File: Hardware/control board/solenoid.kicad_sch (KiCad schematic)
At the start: 7 parts, among them J11 Screw_Terminal_01x02, Q3 NMOS

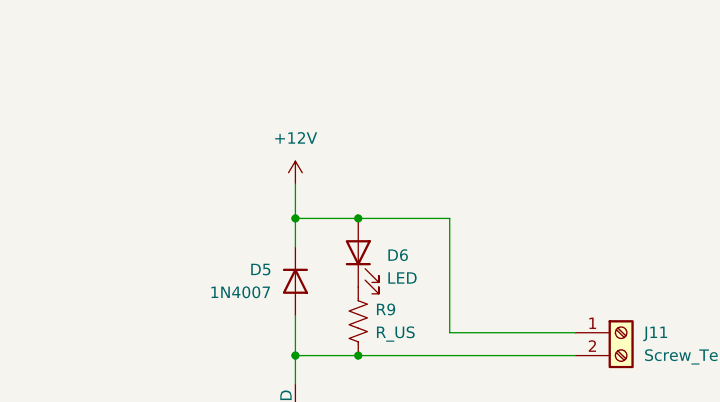
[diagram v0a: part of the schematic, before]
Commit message: added fuses into solenoids/escs
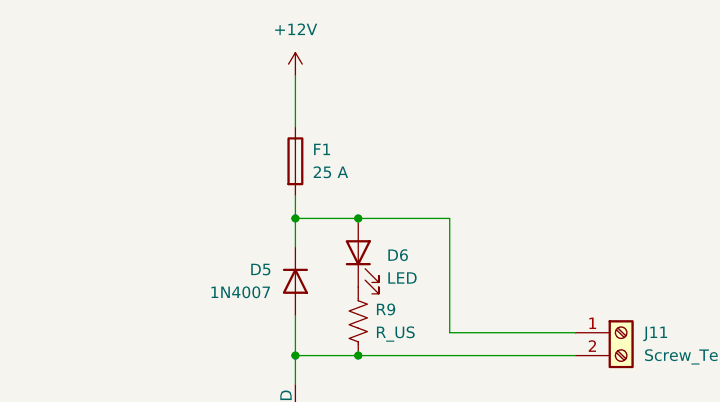
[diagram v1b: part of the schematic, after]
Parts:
- added F1: 25 A, symbol Device:Fuse
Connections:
- net +12V: now also F1.1; no longer D5.1 (K), D6.2 (A), J11.1 (Pin_1)
- new net: D5.1 (K), D6.2 (A), F1.2, J11.1 (Pin_1)
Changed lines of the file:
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@@
 (kicad_sch (version 20230121) (generator eeschema)
   (paper "A4")
+  (junction (at 122.555 75.565) (diameter 0) (color 0 0 0 0)
+  )
   (junction (at 129.54 75.565) (diameter 0) (color 0 0 0 0)
   )
@@
   (junction (at 129.54 90.805) (diameter 0) (color 0 0 0 0)
   )
-  (junction (at 122.555 75.565) (diameter 0) (color 0 0 0 0)
-  )
   (wire (pts (xy 120.015 113.03) (xy 122.555 113.03))
     (stroke (width 0) (type default))
@@
     (stroke (width 0) (type default))
   )
+  (wire (pts (xy 122.555 73.025) (xy 122.555 75.565))
+    (stroke (width 0) (type default))
+  )
   (wire (pts (xy 122.555 104.14) (xy 122.555 113.03))
     (stroke (width 0) (type default))
@@
     (stroke (width 0) (type default))
   )
+  (wire (pts (xy 122.555 59.69) (xy 122.555 65.405))
+    (stroke (width 0) (type default))
+  )
   (wire (pts (xy 139.7 88.265) (xy 153.67 88.265))
-    (stroke (width 0) (type default))
-  )
-  (wire (pts (xy 122.555 71.755) (xy 122.555 75.565))
     (stroke (width 0) (type default))
   )
@@
     (pin "3")
     (instances
-      (project "control board"
-        (path "/cf0863a8-7f64-449b-8eb4-3c06c871fb37"
+      (project "solenoid"
+        (path "/b4ed5960-473e-41d7-9d87-eb439ed22219"
           (reference "Q3") (unit 1)
         )
+      )
+      (project "control board"
+        (path "/cf0863a8-7f64-449b-8eb4-3c06c871fb37"
+          (reference "Q3") (unit 1)
+        )
         (path "/cf0863a8-7f64-449b-8eb4-3c06c871fb37/9fd0b45f-6f46-40af-ae0d-29c33b45e498"
           (reference "Q1") (unit 1)
@@
         (path "/cf0863a8-7f64-449b-8eb4-3c06c871fb37/f39ce93b-3626-4dde-a021-b00a2c8134c7"
           (reference "Q3") (unit 1)
+        )
+      )
+    )
+  )
+  (symbol (lib_id "Device:Fuse") (at 122.555 69.215 0) (unit 1)
+    (in_bom yes) (on_board yes) (dnp no) (fields_autoplaced)
+    (property "Reference" "F1" (at 124.46 67.945 0)
+      (effects (font (size 1.27 1.27)) (justify left))
+    )
+    (property "Value" "25 A" (at 124.46 70.485 0)
+      (effects (font (size 1.27 1.27)) (justify left))
+    )
+    (property "Footprint" "" (at 120.777 69.215 90)
+      (effects (font (size 1.27 1.27)) hide)
+    )
+    (property "Datasheet" "~" (at 122.555 69.215 0)
+      (effects (font (size 1.27 1.27)) hide)
+    )
+    (pin "1")
+    (pin "2")
+    (instances
+      (project "solenoid"
+        (path "/b4ed5960-473e-41d7-9d87-eb439ed22219"
+          (reference "F1") (unit 1)
+        )
+      )
+      (project "control board"
+        (path "/cf0863a8-7f64-449b-8eb4-3c06c871fb37/9fd0b45f-6f46-40af-ae0d-29c33b45e498"
+          (reference "F1") (unit 1)
+        )
+        (path "/cf0863a8-7f64-449b-8eb4-3c06c871fb37/6163a064-c95f-47b6-9c17-0e18c391c233"
+          (reference "F1") (unit 1)
+        )
+        (path "/cf0863a8-7f64-449b-8eb4-3c06c871fb37/f39ce93b-3626-4dde-a021-b00a2c8134c7"
+          (reference "F1") (unit 1)
         )
       )
@@
     (pin "2")
     (instances
-      (project "control board"
-        (path "/cf0863a8-7f64-449b-8eb4-3c06c871fb37"
+      (project "solenoid"
+        (path "/b4ed5960-473e-41d7-9d87-eb439ed22219"
           (reference "D6") (unit 1)
         )
+      )
+      (project "control board"
+        (path "/cf0863a8-7f64-449b-8eb4-3c06c871fb37"
+          (reference "D6") (unit 1)
+        )
         (path "/cf0863a8-7f64-449b-8eb4-3c06c871fb37/9fd0b45f-6f46-40af-ae0d-29c33b45e498"
           (reference "D2") (unit 1)
@@
     (pin "2")
     (instances
-      (project "control board"
-        (path "/cf0863a8-7f64-449b-8eb4-3c06c871fb37"
+      (project "solenoid"
+        (path "/b4ed5960-473e-41d7-9d87-eb439ed22219"
           (reference "J11") (unit 1)
         )
+      )
+      (project "control board"
+        (path "/cf0863a8-7f64-449b-8eb4-3c06c871fb37"
+          (reference "J11") (unit 1)
+        )
         (path "/cf0863a8-7f64-449b-8eb4-3c06c871fb37/9fd0b45f-6f46-40af-ae0d-29c33b45e498"
           (reference "J9") (unit 1)
@@
         (path "/cf0863a8-7f64-449b-8eb4-3c06c871fb37/f39ce93b-3626-4dde-a021-b00a2c8134c7"
           (reference "J11") (unit 1)
-        )
-      )
-    )
-  )
-  (symbol (lib_id "power:+12V") (at 122.555 71.755 0) (unit 1)
-    (in_bom yes) (on_board yes) (dnp no) (fields_autoplaced)
-    (property "Reference" "#PWR08" (at 122.555 75.565 0)
-      (effects (font (size 1.27 1.27)) hide)
-    )
-    (property "Value" "+12V" (at 122.555 66.675 0)
-      (effects (font (size 1.27 1.27)))
-    )
-    (property "Footprint" "" (at 122.555 71.755 0)
-      (effects (font (size 1.27 1.27)) hide)
-    )
-    (property "Datasheet" "" (at 122.555 71.755 0)
-      (effects (font (size 1.27 1.27)) hide)
-    )
-    (pin "1")
-    (instances
-      (project "control board"
-        (path "/cf0863a8-7f64-449b-8eb4-3c06c871fb37"
-          (reference "#PWR08") (unit 1)
-        )
-        (path "/cf0863a8-7f64-449b-8eb4-3c06c871fb37/9fd0b45f-6f46-40af-ae0d-29c33b45e498"
-          (reference "#PWR02") (unit 1)
-        )
-        (path "/cf0863a8-7f64-449b-8eb4-3c06c871fb37/6163a064-c95f-47b6-9c17-0e18c391c233"
-          (reference "#PWR04") (unit 1)
-        )
-        (path "/cf0863a8-7f64-449b-8eb4-3c06c871fb37/f39ce93b-3626-4dde-a021-b00a2c8134c7"
-          (reference "#PWR06") (unit 1)
         )
       )
@@
     (pin "2")
     (instances
-      (project "control board"
-        (path "/cf0863a8-7f64-449b-8eb4-3c06c871fb37"
+      (project "solenoid"
+        (path "/b4ed5960-473e-41d7-9d87-eb439ed22219"
           (reference "R8") (unit 1)
         )
+      )
+      (project "control board"
+        (path "/cf0863a8-7f64-449b-8eb4-3c06c871fb37"
+          (reference "R8") (unit 1)
+        )
         (path "/cf0863a8-7f64-449b-8eb4-3c06c871fb37/9fd0b45f-6f46-40af-ae0d-29c33b45e498"
           (reference "R2") (unit 1)
@@
     (pin "2")
     (instances
+      (project "solenoid"
+        (path "/b4ed5960-473e-41d7-9d87-eb439ed22219"
+          (reference "R9") (unit 1)
+        )
+      )
       (project "control board"
         (path "/cf0863a8-7f64-449b-8eb4-3c06c871fb37"
@@
     (pin "1")
     (instances
+      (project "solenoid"
+        (path "/b4ed5960-473e-41d7-9d87-eb439ed22219"
+          (reference "#PWR09") (unit 1)
+        )
+      )
       (project "control board"
         (path "/cf0863a8-7f64-449b-8eb4-3c06c871fb37"
@@
     (pin "2")
     (instances
-      (project "control board"
-        (path "/cf0863a8-7f64-449b-8eb4-3c06c871fb37"
+      (project "solenoid"
+        (path "/b4ed5960-473e-41d7-9d87-eb439ed22219"
           (reference "R7") (unit 1)
         )
+      )
+      (project "control board"
+        (path "/cf0863a8-7f64-449b-8eb4-3c06c871fb37"
+          (reference "R7") (unit 1)
+        )
         (path "/cf0863a8-7f64-449b-8eb4-3c06c871fb37/9fd0b45f-6f46-40af-ae0d-29c33b45e498"
           (reference "R1") (unit 1)
@@
         (path "/cf0863a8-7f64-449b-8eb4-3c06c871fb37/f39ce93b-3626-4dde-a021-b00a2c8134c7"
           (reference "R7") (unit 1)
+        )
+      )
+    )
+  )
+  (symbol (lib_id "power:+12V") (at 122.555 59.69 0) (unit 1)
+    (in_bom yes) (on_board yes) (dnp no) (fields_autoplaced)
+    (property "Reference" "#PWR01" (at 122.555 63.5 0)
+      (effects (font (size 1.27 1.27)) hide)
+    )
+    (property "Value" "+12V" (at 122.555 54.61 0)
+      (effects (font (size 1.27 1.27)))
+    )
+    (property "Footprint" "" (at 122.555 59.69 0)
+      (effects (font (size 1.27 1.27)) hide)
+    )
+    (property "Datasheet" "" (at 122.555 59.69 0)
+      (effects (font (size 1.27 1.27)) hide)
+    )
+    (pin "1")
+    (instances
+      (project "solenoid"
+        (path "/b4ed5960-473e-41d7-9d87-eb439ed22219"
+          (reference "#PWR01") (unit 1)
+        )
+      )
+      (project "control board"
+        (path "/cf0863a8-7f64-449b-8eb4-3c06c871fb37/9fd0b45f-6f46-40af-ae0d-29c33b45e498"
+          (reference "#PWR01") (unit 1)
+        )
+        (path "/cf0863a8-7f64-449b-8eb4-3c06c871fb37/6163a064-c95f-47b6-9c17-0e18c391c233"
+          (reference "#PWR01") (unit 1)
+        )
+        (path "/cf0863a8-7f64-449b-8eb4-3c06c871fb37/f39ce93b-3626-4dde-a021-b00a2c8134c7"
+          (reference "#PWR01") (unit 1)
         )
       )
@@
     (pin "2")
     (instances
-      (project "control board"
-        (path "/cf0863a8-7f64-449b-8eb4-3c06c871fb37"
+      (project "solenoid"
+        (path "/b4ed5960-473e-41d7-9d87-eb439ed22219"
+          (reference "D5") (unit 1)
+        )
+      )
+      (project "control board"
+        (path "/cf0863a8-7f64-449b-8eb4-3c06c871fb37"

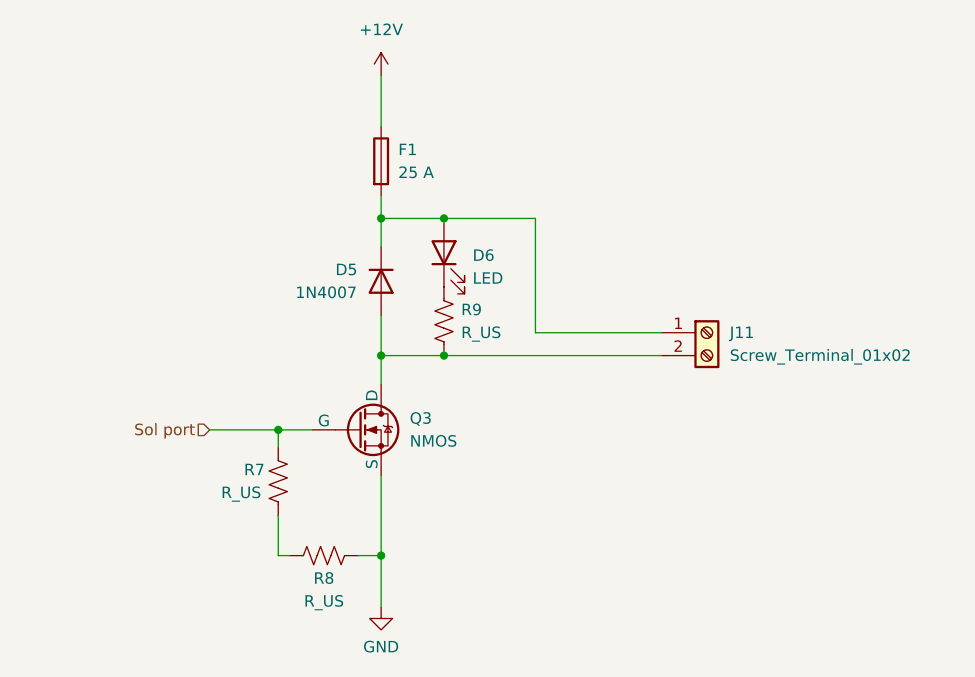
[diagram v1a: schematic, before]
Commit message: renamed boards
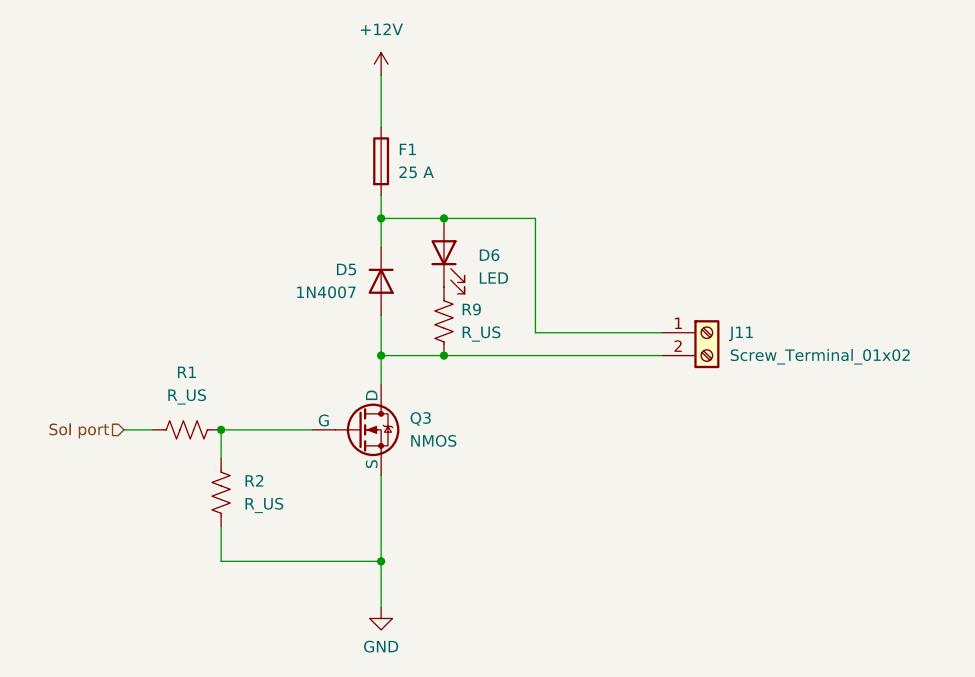
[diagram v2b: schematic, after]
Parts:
- removed R7, R8: R_US, symbol Device:R_US
- added R1, R2: R_US, symbol Device:R_US
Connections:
- net GND: now also R2.2
- net Sol port: now also R1.1; no longer Q3.2 (G)
- new net: Q3.2 (G), R1.2, R2.1
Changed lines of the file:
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@@
   (junction (at 122.555 90.805) (diameter 0) (color 0 0 0 0)
   )
-  (junction (at 122.555 113.03) (diameter 0) (color 0 0 0 0)
-  )
-  (junction (at 111.125 99.06) (diameter 0) (color 0 0 0 0)
+  (junction (at 104.775 99.06) (diameter 0) (color 0 0 0 0)
+  )
+  (junction (at 122.555 113.665) (diameter 0) (color 0 0 0 0)
   )
   (junction (at 129.54 90.805) (diameter 0) (color 0 0 0 0)
   )
-  (wire (pts (xy 120.015 113.03) (xy 122.555 113.03))
+  (wire (pts (xy 104.775 109.855) (xy 104.775 113.665))
+    (stroke (width 0) (type default))
+  )
+  (wire (pts (xy 104.775 99.06) (xy 104.775 102.235))
     (stroke (width 0) (type default))
   )
@@
     (stroke (width 0) (type default))
   )
-  (wire (pts (xy 111.125 108.585) (xy 111.125 113.03))
-    (stroke (width 0) (type default))
-  )
-  (wire (pts (xy 111.125 113.03) (xy 112.395 113.03))
+  (wire (pts (xy 104.775 99.06) (xy 114.935 99.06))
+    (stroke (width 0) (type default))
+  )
+  (wire (pts (xy 104.775 113.665) (xy 122.555 113.665))
     (stroke (width 0) (type default))
   )
@@
     (stroke (width 0) (type default))
   )
-  (wire (pts (xy 103.505 99.06) (xy 111.125 99.06))
+  (wire (pts (xy 93.98 99.06) (xy 97.155 99.06))
     (stroke (width 0) (type default))
   )
@@
     (stroke (width 0) (type default))
   )
-  (wire (pts (xy 111.125 99.06) (xy 111.125 100.965))
-    (stroke (width 0) (type default))
-  )
   (wire (pts (xy 122.555 73.025) (xy 122.555 75.565))
     (stroke (width 0) (type default))
   )
-  (wire (pts (xy 122.555 104.14) (xy 122.555 113.03))
-    (stroke (width 0) (type default))
-  )
   (wire (pts (xy 129.54 75.565) (xy 139.7 75.565))
     (stroke (width 0) (type default))
@@
     (stroke (width 0) (type default))
   )
-  (wire (pts (xy 111.125 99.06) (xy 114.935 99.06))
-    (stroke (width 0) (type default))
-  )
   (wire (pts (xy 122.555 75.565) (xy 129.54 75.565))
     (stroke (width 0) (type default))
   )
+  (wire (pts (xy 122.555 104.14) (xy 122.555 113.665))
+    (stroke (width 0) (type default))
+  )
+  (wire (pts (xy 122.555 113.665) (xy 122.555 118.745))
+    (stroke (width 0) (type default))
+  )
   (wire (pts (xy 122.555 75.565) (xy 122.555 78.74))
     (stroke (width 0) (type default))
@@
     (stroke (width 0) (type default))
   )
-  (wire (pts (xy 122.555 113.03) (xy 122.555 118.745))
-    (stroke (width 0) (type default))
-  )
-  (hierarchical_label "Sol port" (shape input) (at 103.505 99.06 180) (fields_autoplaced)
+  (hierarchical_label "Sol port" (shape input) (at 93.98 99.06 180) (fields_autoplaced)
     (effects (font (size 1.27 1.27)) (justify right))
   )
@@
   (symbol (lib_id "Device:LED") (at 129.54 79.375 90) (unit 1)
     (in_bom yes) (on_board yes) (dnp no) (fields_autoplaced)
-    (property "Reference" "D6" (at 132.715 79.6925 90)
+    (property "Reference" "D6" (at 133.35 79.6925 90)
       (effects (font (size 1.27 1.27)) (justify right))
     )
-    (property "Value" "LED" (at 132.715 82.2325 90)
+    (property "Value" "LED" (at 133.35 82.2325 90)
       (effects (font (size 1.27 1.27)) (justify right))
     )
@@
         )
         (path "/cf0863a8-7f64-449b-8eb4-3c06c871fb37/9fd0b45f-6f46-40af-ae0d-29c33b45e498"
-          (reference "D2") (unit 1)
+          (reference "Green") (unit 1)
         )
         (path "/cf0863a8-7f64-449b-8eb4-3c06c871fb37/6163a064-c95f-47b6-9c17-0e18c391c233"
@@
     )
   )
-  (symbol (lib_id "Device:R_US") (at 116.205 113.03 270) (unit 1)
-    (in_bom yes) (on_board yes) (dnp no)
-    (property "Reference" "R8" (at 116.205 115.57 90)
+  (symbol (lib_id "Device:R_US") (at 100.965 99.06 90) (unit 1)
+    (in_bom yes) (on_board yes) (dnp no) (fields_autoplaced)
+    (property "Reference" "R1" (at 100.965 92.71 90)
       (effects (font (size 1.27 1.27)))
     )
-    (property "Value" "R_US" (at 116.205 118.11 90)
+    (property "Value" "R_US" (at 100.965 95.25 90)
       (effects (font (size 1.27 1.27)))
     )
-    (property "Footprint" "" (at 115.951 114.046 90)
-      (effects (font (size 1.27 1.27)) hide)
-    )
-    (property "Datasheet" "~" (at 116.205 113.03 0)
-      (effects (font (size 1.27 1.27)) hide)
-    )
-    (pin "1")
-    (pin "2")
-    (instances
-      (project "solenoid"
-        (path "/b4ed5960-473e-41d7-9d87-eb439ed22219"
-          (reference "R8") (unit 1)
-        )
-      )
-      (project "control board"
-        (path "/cf0863a8-7f64-449b-8eb4-3c06c871fb37"
-          (reference "R8") (unit 1)
-        )
+    (property "Footprint" "" (at 101.219 98.044 90)
+      (effects (font (size 1.27 1.27)) hide)
+    )
+    (property "Datasheet" "~" (at 100.965 99.06 0)
+      (effects (font (size 1.27 1.27)) hide)
+    )
+    (pin "1")
+    (pin "2")
+    (instances
+      (project "control board"
+        (path "/cf0863a8-7f64-449b-8eb4-3c06c871fb37/9fd0b45f-6f46-40af-ae0d-29c33b45e498"
+          (reference "R1") (unit 1)
+        )
+        (path "/cf0863a8-7f64-449b-8eb4-3c06c871fb37/6163a064-c95f-47b6-9c17-0e18c391c233"
+          (reference "R3") (unit 1)
+        )
+        (path "/cf0863a8-7f64-449b-8eb4-3c06c871fb37/f39ce93b-3626-4dde-a021-b00a2c8134c7"
+          (reference "R7") (unit 1)
+        )
+      )
+    )
+  )
+  (symbol (lib_id "Device:R_US") (at 104.775 106.045 0) (unit 1)
+    (in_bom yes) (on_board yes) (dnp no) (fields_autoplaced)
+    (property "Reference" "R2" (at 107.315 104.775 0)
+      (effects (font (size 1.27 1.27)) (justify left))
+    )
+    (property "Value" "R_US" (at 107.315 107.315 0)
+      (effects (font (size 1.27 1.27)) (justify left))
+    )
+    (property "Footprint" "" (at 105.791 106.299 90)
+      (effects (font (size 1.27 1.27)) hide)
+    )
+    (property "Datasheet" "~" (at 104.775 106.045 0)
+      (effects (font (size 1.27 1.27)) hide)
+    )
+    (pin "1")
+    (pin "2")
+    (instances
+      (project "control board"
         (path "/cf0863a8-7f64-449b-8eb4-3c06c871fb37/9fd0b45f-6f46-40af-ae0d-29c33b45e498"
           (reference "R2") (unit 1)
@@
         )
       )
-    )
-  )
-  (symbol (lib_id "Device:R_US") (at 111.125 104.775 0) (unit 1)
-    (in_bom yes) (on_board yes) (dnp no)
-    (property "Reference" "R7" (at 107.315 103.505 0)
-      (effects (font (size 1.27 1.27)) (justify left))
-    )
-    (property "Value" "R_US" (at 104.775 106.045 0)
-      (effects (font (size 1.27 1.27)) (justify left))
-    )
-    (property "Footprint" "" (at 112.141 105.029 90)
-      (effects (font (size 1.27 1.27)) hide)
-    )
-    (property "Datasheet" "~" (at 111.125 104.775 0)
-      (effects (font (size 1.27 1.27)) hide)
-    )
-    (pin "1")
-    (pin "2")
-    (instances
-      (project "solenoid"
-        (path "/b4ed5960-473e-41d7-9d87-eb439ed22219"
-          (reference "R7") (unit 1)
-        )
-      )
-      (project "control board"
-        (path "/cf0863a8-7f64-449b-8eb4-3c06c871fb37"
-          (reference "R7") (unit 1)
-        )
-        (path "/cf0863a8-7f64-449b-8eb4-3c06c871fb37/9fd0b45f-6f46-40af-ae0d-29c33b45e498"
-          (reference "R1") (unit 1)
-        )
-        (path "/cf0863a8-7f64-449b-8eb4-3c06c871fb37/6163a064-c95f-47b6-9c17-0e18c391c233"
-          (reference "R3") (unit 1)
-        )
-        (path "/cf0863a8-7f64-449b-8eb4-3c06c871fb37/f39ce93b-3626-4dde-a021-b00a2c8134c7"
-          (reference "R7") (unit 1)
-        )
-      )

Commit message: added resistor values to solenoid boards
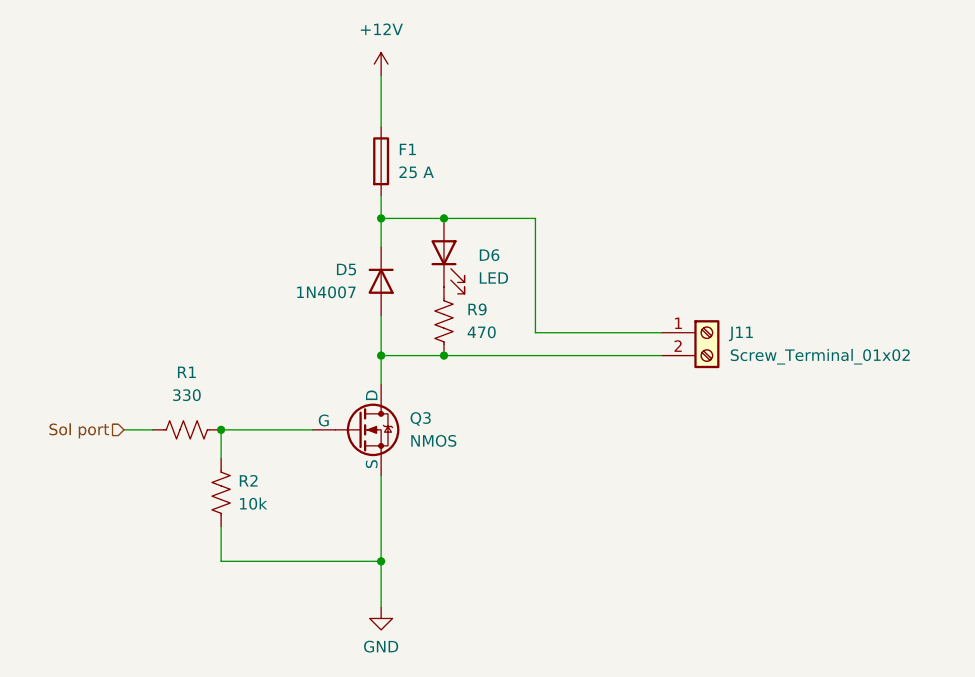
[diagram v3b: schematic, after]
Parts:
- R1: value R_US -> 330
- R2: value R_US -> 10k
- R9: value R_US -> 470
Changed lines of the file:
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@@
       (effects (font (size 1.27 1.27)))
     )
-    (property "Value" "R_US" (at 100.965 95.25 90)
+    (property "Value" "330" (at 100.965 95.25 90)
       (effects (font (size 1.27 1.27)))
     )
@@
   (symbol (lib_id "Device:R_US") (at 104.775 106.045 0) (unit 1)
     (in_bom yes) (on_board yes) (dnp no) (fields_autoplaced)
-    (property "Reference" "R2" (at 107.315 104.775 0)
+    (property "Reference" "R2" (at 106.68 104.775 0)
       (effects (font (size 1.27 1.27)) (justify left))
     )
-    (property "Value" "R_US" (at 107.315 107.315 0)
+    (property "Value" "10k" (at 106.68 107.315 0)
       (effects (font (size 1.27 1.27)) (justify left))
     )
@@
   (symbol (lib_id "Device:R_US") (at 129.54 86.995 0) (unit 1)
     (in_bom yes) (on_board yes) (dnp no) (fields_autoplaced)
-    (property "Reference" "R9" (at 131.445 85.725 0)
+    (property "Reference" "R9" (at 132.08 85.725 0)
       (effects (font (size 1.27 1.27)) (justify left))
     )
-    (property "Value" "R_US" (at 131.445 88.265 0)
+    (property "Value" "470" (at 132.08 88.265 0)
       (effects (font (size 1.27 1.27)) (justify left))
     )
